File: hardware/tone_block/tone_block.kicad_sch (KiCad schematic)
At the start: 38 parts, among them J1 I/O, Q1 RS32716R, Q2 LBSS84LT1G, SW1 DPDT, U1 TLV170IDBVR

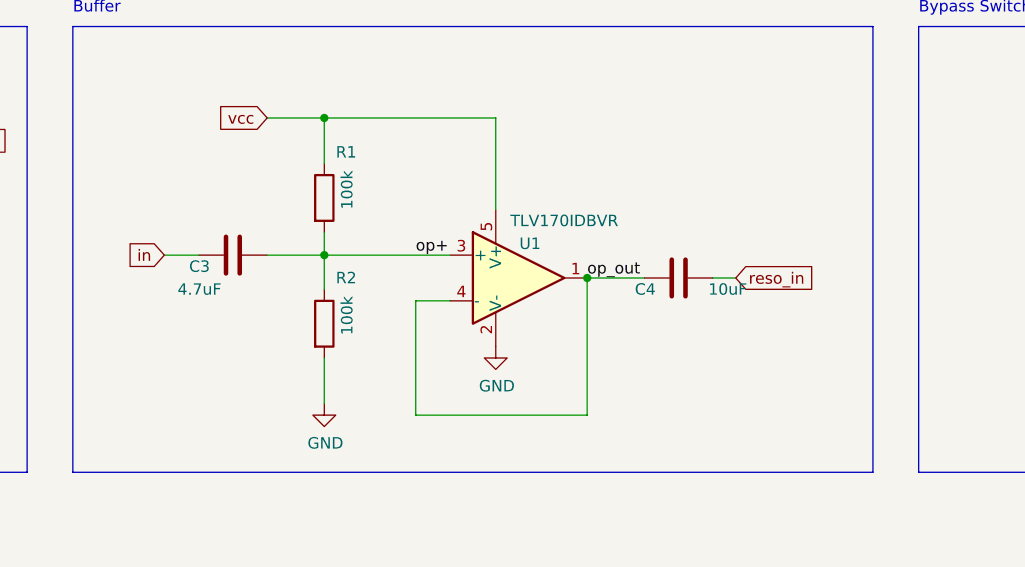
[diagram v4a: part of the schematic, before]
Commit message: JLCPCB components optimization
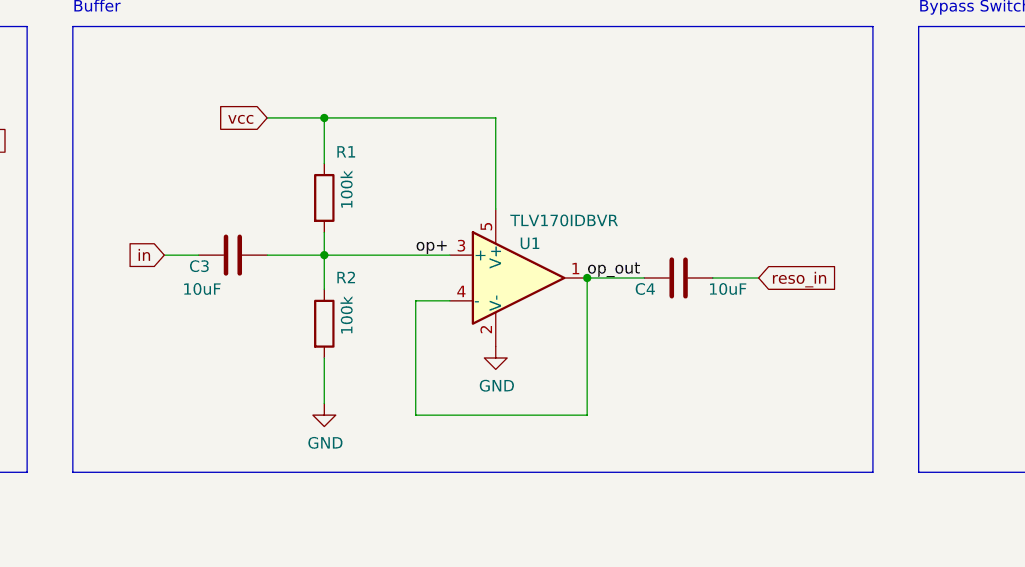
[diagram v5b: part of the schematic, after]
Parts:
- C1: footprint Capacitor_SMD:C_0603_1608Metric -> Capacitor_SMD:C_0805_2012Metric
- C10, C11, C12, C13, C5, C6, C7, C8, C9: footprint Resistor_SMD:R_0402_1005Metric -> Capacitor_SMD:C_0603_1608Metric
- C3: value 4.7uF -> 10uF; footprint Capacitor_SMD:C_0603_1608Metric -> Capacitor_SMD:C_0805_2012Metric
- C4: footprint Resistor_SMD:R_0603_1608Metric -> Capacitor_SMD:C_0805_2012Metric
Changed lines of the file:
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@@
     (stroke (width 0) (type default) (color 0 0 0 0))
   )
-  (wire (pts (xy 148.59 135.89) (xy 151.13 135.89))
+  (wire (pts (xy 148.59 135.89) (xy 153.67 135.89))
     (stroke (width 0) (type default) (color 0 0 0 0))
   )
@@
     )
   )
-  (global_label "reso_in" (shape input) (at 151.13 135.89 0) (fields_autoplaced)
+  (global_label "reso_in" (shape input) (at 153.67 135.89 0) (fields_autoplaced)
     (effects (font (size 1.27 1.27)) (justify left))
-    (property "Intersheet References" "${INTERSHEET_REFS}" (id 0) (at 160.2275 135.8106 0)
+    (property "Intersheet References" "${INTERSHEET_REFS}" (id 0) (at 162.7675 135.8106 0)
       (effects (font (size 1.27 1.27)) (justify left) hide)
     )
@@
       (effects (font (size 1.27 1.27)) hide)
     )
-    (property "Footprint" "Resistor_SMD:R_0402_1005Metric" (id 2) (at 218.44 52.07 0)
+    (property "Footprint" "Capacitor_SMD:C_0603_1608Metric" (id 2) (at 218.44 52.07 0)
       (effects (font (size 1.27 1.27)) hide)
     )
@@
       (effects (font (size 1.27 1.27)) (justify right))
     )
-    (property "Value" "4.7uF" (id 1) (at 93.98 137.16 90)
-      (effects (font (size 1.27 1.27)) (justify right))
-    )
-    (property "Footprint" "Capacitor_SMD:C_0603_1608Metric" (id 2) (at 91.44 132.3848 0)
+    (property "Value" "10uF" (id 1) (at 93.98 137.16 90)
+      (effects (font (size 1.27 1.27)) (justify right))
+    )
+    (property "Footprint" "Capacitor_SMD:C_0805_2012Metric" (id 2) (at 91.44 132.3848 0)
       (effects (font (size 1.27 1.27)) hide)
     )
@@
       (effects (font (size 1.27 1.27)) hide)
     )
-    (property "Footprint" "Resistor_SMD:R_0402_1005Metric" (id 2) (at 231.14 45.72 0)
+    (property "Footprint" "Capacitor_SMD:C_0603_1608Metric" (id 2) (at 231.14 45.72 0)
       (effects (font (size 1.27 1.27)) hide)
     )
@@
       (effects (font (size 1.27 1.27)) hide)
     )
-    (property "Footprint" "Resistor_SMD:R_0402_1005Metric" (id 2) (at 224.79 45.72 0)
+    (property "Footprint" "Capacitor_SMD:C_0603_1608Metric" (id 2) (at 224.79 45.72 0)
       (effects (font (size 1.27 1.27)) hide)
     )
@@
       (effects (font (size 1.27 1.27)) hide)
     )
-    (property "Footprint" "Resistor_SMD:R_0402_1005Metric" (id 2) (at 222.25 58.42 0)
+    (property "Footprint" "Capacitor_SMD:C_0603_1608Metric" (id 2) (at 222.25 58.42 0)
       (effects (font (size 1.27 1.27)) hide)
     )
@@
       (effects (font (size 1.27 1.27)) hide)
     )
-    (property "Footprint" "Resistor_SMD:R_0402_1005Metric" (id 2) (at 222.25 64.77 0)
+    (property "Footprint" "Capacitor_SMD:C_0603_1608Metric" (id 2) (at 222.25 64.77 0)
       (effects (font (size 1.27 1.27)) hide)
     )
@@
       (effects (font (size 1.27 1.27)) hide)
     )
-    (property "Footprint" "Resistor_SMD:R_0402_1005Metric" (id 2) (at 222.25 68.58 0)
+    (property "Footprint" "Capacitor_SMD:C_0603_1608Metric" (id 2) (at 222.25 68.58 0)
       (effects (font (size 1.27 1.27)) hide)
     )
@@
       (effects (font (size 1.27 1.27)) hide)
     )
-    (property "Footprint" "Resistor_SMD:R_0402_1005Metric" (id 2) (at 218.44 45.72 0)
+    (property "Footprint" "Capacitor_SMD:C_0603_1608Metric" (id 2) (at 218.44 45.72 0)
       (effects (font (size 1.27 1.27)) hide)
     )
@@
       (effects (font (size 1.27 1.27)) (justify right))
     )
-    (property "Footprint" "Capacitor_SMD:C_0603_1608Metric" (id 2) (at 53.0352 125.73 0)
+    (property "Footprint" "Capacitor_SMD:C_0805_2012Metric" (id 2) (at 53.0352 125.73 0)
       (effects (font (size 1.27 1.27)) hide)
     )
@@
       (effects (font (size 1.27 1.27)) hide)
     )
-    (property "Footprint" "Resistor_SMD:R_0402_1005Metric" (id 2) (at 224.79 52.07 0)
+    (property "Footprint" "Capacitor_SMD:C_0603_1608Metric" (id 2) (at 224.79 52.07 0)
       (effects (font (size 1.27 1.27)) hide)
     )
@@
       (effects (font (size 1.27 1.27)) hide)
     )
-    (property "Footprint" "Resistor_SMD:R_0402_1005Metric" (id 2) (at 212.09 45.72 0)
+    (property "Footprint" "Capacitor_SMD:C_0603_1608Metric" (id 2) (at 212.09 45.72 0)
       (effects (font (size 1.27 1.27)) hide)
     )
@@
       (effects (font (size 1.27 1.27)) (justify right))
     )
-    (property "Footprint" "Resistor_SMD:R_0603_1608Metric" (id 2) (at 140.97 134.9248 0)
+    (property "Footprint" "Capacitor_SMD:C_0805_2012Metric" (id 2) (at 140.97 134.9248 0)
       (effects (font (size 1.27 1.27)) hide)
     )
@@
     )
     (path "/be65158e-33cb-4d1a-9bfc-bbe28283e565"
-      (reference "C1") (unit 1) (value "4.7uF") (footprint "Capacitor_SMD:C_0603_1608Metric")
+      (reference "C1") (unit 1) (value "4.7uF") (footprint "Capacitor_SMD:C_0805_2012Metric")
     )
     (path "/5d9562af-9a86-40d8-a6f0-7078717c93b7"
@@
     )
     (path "/41c313f9-ac50-43d9-af87-7561a5ffc20c"
-      (reference "C3") (unit 1) (value "4.7uF") (footprint "Capacitor_SMD:C_0603_1608Metric")
+      (reference "C3") (unit 1) (value "10uF") (footprint "Capacitor_SMD:C_0805_2012Metric")
     )
     (path "/f156067d-13ff-4a50-a39a-c4ddaa8a74d6"
-      (reference "C4") (unit 1) (value "10uF") (footprint "Resistor_SMD:R_0603_1608Metric")
+      (reference "C4") (unit 1) (value "10uF") (footprint "Capacitor_SMD:C_0805_2012Metric")
     )
     (path "/ef74b382-bd99-4cb0-9568-575712c83436"
-      (reference "C5") (unit 1) (value "47nF") (footprint "Resistor_SMD:R_0402_1005Metric")
+      (reference "C5") (unit 1) (value "47nF") (footprint "Capacitor_SMD:C_0603_1608Metric")
     )
     (path "/38d14fe5-876b-42c2-98f2-36004534d0d9"
-      (reference "C6") (unit 1) (value "47nF") (footprint "Resistor_SMD:R_0402_1005Metric")
+      (reference "C6") (unit 1) (value "47nF") (footprint "Capacitor_SMD:C_0603_1608Metric")
     )
     (path "/582e6278-b5e0-4e16-a0ec-0e5c1cc98a96"
-      (reference "C7") (unit 1) (value "47nF") (footprint "Resistor_SMD:R_0402_1005Metric")
+      (reference "C7") (unit 1) (value "47nF") (footprint "Capacitor_SMD:C_0603_1608Metric")
     )
     (path "/684dc39e-476f-45c2-9396-f5ebd24b969d"
-      (reference "C8") (unit 1) (value "47nF") (footprint "Resistor_SMD:R_0402_1005Metric")
+      (reference "C8") (unit 1) (value "47nF") (footprint "Capacitor_SMD:C_0603_1608Metric")
     )
     (path "/9fd407b7-d7b5-4734-9240-5955d7ffea2a"
-      (reference "C9") (unit 1) (value "47nF") (footprint "Resistor_SMD:R_0402_1005Metric")
+      (reference "C9") (unit 1) (value "47nF") (footprint "Capacitor_SMD:C_0603_1608Metric")
     )
     (path "/b9cb5bb2-5343-4e30-8548-c85fd05beaca"
-      (reference "C10") (unit 1) (value "47nF") (footprint "Resistor_SMD:R_0402_1005Metric")
+      (reference "C10") (unit 1) (value "47nF") (footprint "Capacitor_SMD:C_0603_1608Metric")
     )
     (path "/c7cb2b5e-4747-4e22-a64c-df5b1348417b"
-      (reference "C11") (unit 1) (value "47nF") (footprint "Resistor_SMD:R_0402_1005Metric")
+      (reference "C11") (unit 1) (value "47nF") (footprint "Capacitor_SMD:C_0603_1608Metric")
     )
     (path "/52b1a3f8-d44b-43c0-9c99-c88649ca3e94"
-      (reference "C12") (unit 1) (value "47nF") (footprint "Resistor_SMD:R_0402_1005Metric")
+      (reference "C12") (unit 1) (value "47nF") (footprint "Capacitor_SMD:C_0603_1608Metric")
     )
     (path "/4cf3af7e-e82c-4e46-8a14-d28848d0996a"
-      (reference "C13") (unit 1) (value "47nF") (footprint "Resistor_SMD:R_0402_1005Metric")
+      (reference "C13") (unit 1) (value "47nF") (footprint "Capacitor_SMD:C_0603_1608Metric")
     )
     (path "/00000000-0000-0000-0000-0000611d5413"

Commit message: Added LCSC part numbers
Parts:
- C1: LCSC Part Number (none) -> C1779
- C10, C11, C12, C13, C5, C6, C7, C8, C9: LCSC Part Number (none) -> C1622
- C2: LCSC Part Number (none) -> C1525
- C3, C4: LCSC Part Number (none) -> C440198
- Q2: LCSC Part Number (none) -> C8492
- R1, R2: LCSC Part Number (none) -> C25741
- R10, R11, R12, R13, R14, R15, R16, R3, R4, R5, R6, R7, R9: LCSC Part Number (none) -> C25104
- R8: LCSC Part Number (none) -> C25900
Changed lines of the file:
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@@
+      (effects (font (size 1.27 1.27)) hide)
+    )
+    (property "LCSC Part Number" "C25900" (id 4) (at 209.55 30.48 0)
       (effects (font (size 1.27 1.27)) hide)
     )
@@
       (effects (font (size 1.27 1.27)) hide)
     )
+    (property "LCSC Part Number" "C25104" (id 4) (at 138.43 35.56 0)
+      (effects (font (size 1.27 1.27)) hide)
+    )
     (pin "1")
     (pin "2")
@@
     )
     (property "Datasheet" "~" (id 3) (at 176.53 43.18 0)
+      (effects (font (size 1.27 1.27)) hide)
+    )
+    (property "LCSC Part Number" "C25104" (id 4) (at 176.53 43.18 0)
       (effects (font (size 1.27 1.27)) hide)
     )
@@
       (effects (font (size 1.27 1.27)) hide)
     )
+    (property "LCSC Part Number" "C25104" (id 4) (at 138.43 50.8 0)
+      (effects (font (size 1.27 1.27)) hide)
+    )
     (pin "1")
     (pin "2")
@@
       (effects (font (size 1.27 1.27)) hide)
     )
+    (property "LCSC Part Number" "C25104" (id 4) (at 176.53 38.1 0)
+      (effects (font (size 1.27 1.27)) hide)
+    )
     (pin "1")
     (pin "2")
@@
       (effects (font (size 1.27 1.27)) hide)
     )
+    (property "LCSC Part Number" "C1622" (id 4) (at 218.44 52.07 0)
+      (effects (font (size 1.27 1.27)) hide)
+    )
     (pin "1")
     (pin "2")
@@
       (effects (font (size 1.27 1.27)) hide)
     )
+    (property "LCSC Part Number" "C25741" (id 4) (at 105.41 127 0)
+      (effects (font (size 1.27 1.27)) hide)
+    )
     (pin "1")
     (pin "2")
@@
       (effects (font (size 1.27 1.27)) hide)
     )
+    (property "LCSC Part Number" "C440198" (id 4) (at 95.25 133.35 0)
+      (effects (font (size 1.27 1.27)) hide)
+    )
     (pin "1")
     (pin "2")
@@
     )
     (property "Datasheet" "~" (id 3) (at 153.67 50.8 0)
+      (effects (font (size 1.27 1.27)) hide)
+    )
+    (property "LCSC Part Number" "C25104" (id 4) (at 153.67 50.8 0)
       (effects (font (size 1.27 1.27)) hide)
     )
@@
       (effects (font (size 1.27 1.27)) hide)
     )
+    (property "LCSC Part Number" "C1622" (id 4) (at 231.14 45.72 0)
+      (effects (font (size 1.27 1.27)) hide)
+    )
     (pin "1")
     (pin "2")
@@
       (effects (font (size 1.27 1.27)) hide)
     )
+    (property "LCSC Part Number" "C1622" (id 4) (at 224.79 45.72 0)
+      (effects (font (size 1.27 1.27)) hide)
+    )
     (pin "1")
     (pin "2")
@@
     )
     (property "Datasheet" "~" (id 3) (at 222.25 58.42 0)
+      (effects (font (size 1.27 1.27)) hide)
+    )
+    (property "LCSC Part Number" "C1622" (id 4) (at 222.25 58.42 0)
       (effects (font (size 1.27 1.27)) hide)
     )
@@
       (effects (font (size 1.27 1.27)) hide)
     )
+    (property "LCSC Part Number" "C8492" (id 4) (at 40.64 123.19 0)
+      (effects (font (size 1.27 1.27)) hide)
+    )
     (pin "1")
     (pin "2")
@@
     )
     (property "Datasheet" "~" (id 3) (at 60.96 129.54 0)
+      (effects (font (size 1.27 1.27)) hide)
+    )
+    (property "LCSC Part Number" "C1525" (id 4) (at 60.96 129.54 0)
       (effects (font (size 1.27 1.27)) hide)
     )
@@
       (effects (font (size 1.27 1.27)) hide)
     )
+    (property "LCSC Part Number" "C1622" (id 4) (at 222.25 64.77 0)
+      (effects (font (size 1.27 1.27)) hide)
+    )
     (pin "1")
     (pin "2")
@@
     )
     (property "Datasheet" "~" (id 3) (at 105.41 140.97 0)
+      (effects (font (size 1.27 1.27)) hide)
+    )
+    (property "LCSC Part Number" "C25741" (id 4) (at 105.41 140.97 0)
       (effects (font (size 1.27 1.27)) hide)
     )
@@
       (effects (font (size 1.27 1.27)) hide)
     )
+    (property "LCSC Part Number" "C25104" (id 4) (at 138.43 45.72 0)
+      (effects (font (size 1.27 1.27)) hide)
+    )
     (pin "1")
     (pin "2")
@@
       (effects (font (size 1.27 1.27)) hide)
     )
+    (property "LCSC Part Number" "C1622" (id 4) (at 222.25 68.58 0)
+      (effects (font (size 1.27 1.27)) hide)
+    )
     (pin "1")
     (pin "2")
@@
     )
     (property "Datasheet" "~" (id 3) (at 176.53 48.26 0)
+      (effects (font (size 1.27 1.27)) hide)
+    )
+    (property "LCSC Part Number" "C25104" (id 4) (at 176.53 48.26 0)
       (effects (font (size 1.27 1.27)) hide)
     )
@@
       (effects (font (size 1.27 1.27)) hide)
     )
+    (property "LCSC Part Number" "C25104" (id 4) (at 146.05 50.8 0)
+      (effects (font (size 1.27 1.27)) hide)
+    )
     (pin "1")
     (pin "2")
@@
       (effects (font (size 1.27 1.27)) hide)
     )
+    (property "LCSC Part Number" "C1622" (id 4) (at 218.44 45.72 0)
+      (effects (font (size 1.27 1.27)) hide)
+    )
     (pin "1")
     (pin "2")
@@
     )
     (property "Datasheet" "~" (id 3) (at 52.07 129.54 0)
+      (effects (font (size 1.27 1.27)) hide)
+    )
+    (property "LCSC Part Number" "C1779" (id 4) (at 52.07 129.54 0)
       (effects (font (size 1.27 1.27)) hide)
     )
@@
       (effects (font (size 1.27 1.27)) hide)
     )
+    (property "LCSC Part Number" "C25104" (id 4) (at 163.83 48.26 0)
+      (effects (font (size 1.27 1.27)) hide)
+    )
     (pin "1")
     (pin "2")
@@
     )
     (property "Datasheet" "~" (id 3) (at 224.79 52.07 0)
+      (effects (font (size 1.27 1.27)) hide)
+    )
+    (property "LCSC Part Number" "C1622" (id 4) (at 224.79 52.07 0)
       (effects (font (size 1.27 1.27)) hide)
     )
@@
       (effects (font (size 1.27 1.27)) hide)
     )
+    (property "LCSC Part Number" "C25104" (id 4) (at 138.43 40.64 0)
+      (effects (font (size 1.27 1.27)) hide)
+    )
     (pin "1")
     (pin "2")
@@
     )
     (property "Datasheet" "~" (id 3) (at 176.53 53.34 0)
+      (effects (font (size 1.27 1.27)) hide)
+    )
+    (property "LCSC Part Number" "C25104" (id 4) (at 176.53 53.34 0)
       (effects (font (size 1.27 1.27)) hide)
     )
@@
       (effects (font (size 1.27 1.27)) hide)
     )
+    (property "LCSC Part Number" "C25104" (id 4) (at 146.05 45.72 0)
+      (effects (font (size 1.27 1.27)) hide)
+    )
     (pin "1")
     (pin "2")
@@
       (effects (font (size 1.27 1.27)) hide)
     )
+    (property "LCSC Part Number" "C1622" (id 4) (at 212.09 45.72 0)
+      (effects (font (size 1.27 1.27)) hide)
+    )
     (pin "1")
     (pin "2")
@@
       (effects (font (size 1.27 1.27)) hide)
     )
+    (property "LCSC Part Number" "C25104" (id 4) (at 163.83 53.34 0)
+      (effects (font (size 1.27 1.27)) hide)
+    )
     (pin "1")
     (pin "2")
@@
       (effects (font (size 1.27 1.27)) hide)
     )
+    (property "LCSC Part Number" "C440198" (id 4) (at 144.78 135.89 0)
+      (effects (font (size 1.27 1.27)) hide)
+    )

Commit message: This is it! v2.0
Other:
- note added: "Capacitor network (all 47nF ±10%)"
- note added: "Resistor network (all 330Ω ±1%)"
- note removed: "Capacitor network (all 47nF COG ±5%)"
- note removed: "Resistor network (all 330Ω ±0.1%)"
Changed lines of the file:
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@@
     (effects (font (size 1.27 1.27)) (justify left bottom))
   )
-  (text "Capacitor network (all 47nF COG ±5%)" (at 204.47 41.91 0)
+  (text "Capacitor network (all 47nF ±10%)" (at 205.74 41.91 0)
     (effects (font (size 1.27 1.27)) (justify left bottom))
   )
@@
     (effects (font (size 1.27 1.27)) (justify left bottom))
   )
-  (text "Resistor network (all 330Ω ±0.1%)" (at 144.78 27.94 0)
+  (text "Resistor network (all 330Ω ±1%)" (at 144.78 27.94 0)
     (effects (font (size 1.27 1.27)) (justify left bottom))
   )
